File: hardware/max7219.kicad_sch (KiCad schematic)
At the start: 4 parts, among them U5 UDN2981A, U6 MAX7219, U7 ULN2803A, U8 74HC540

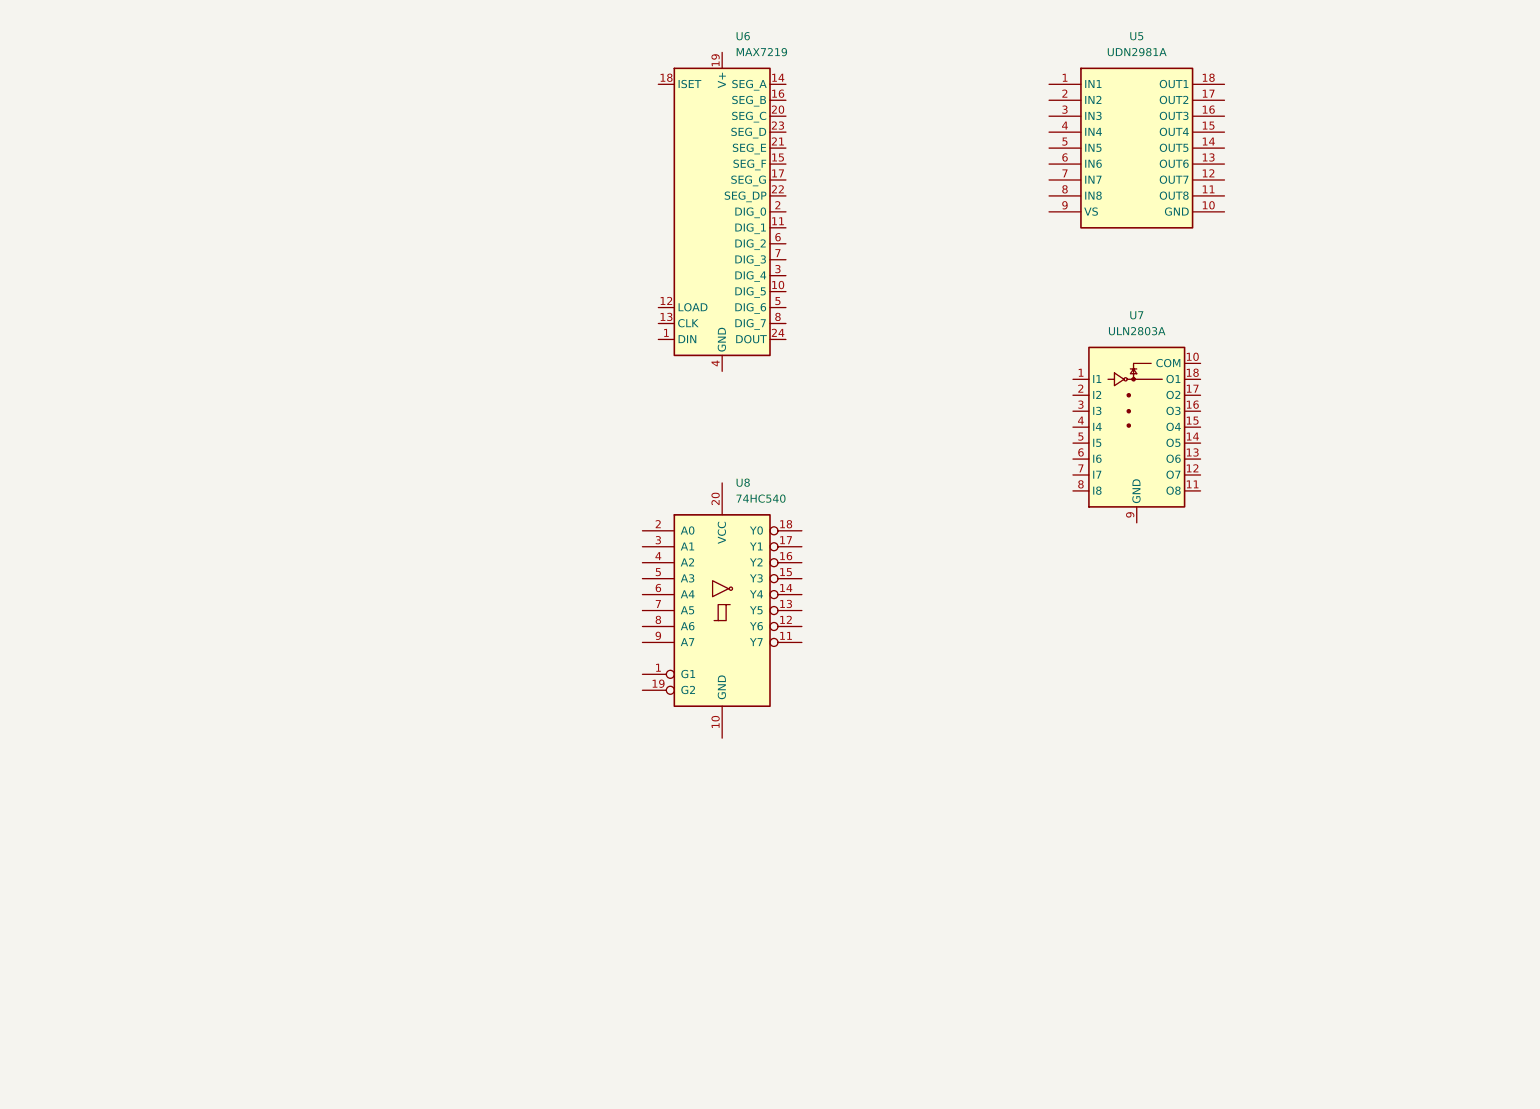
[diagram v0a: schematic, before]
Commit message: Hardware: Rename Temp to RTC-Sensor and Update Schematics
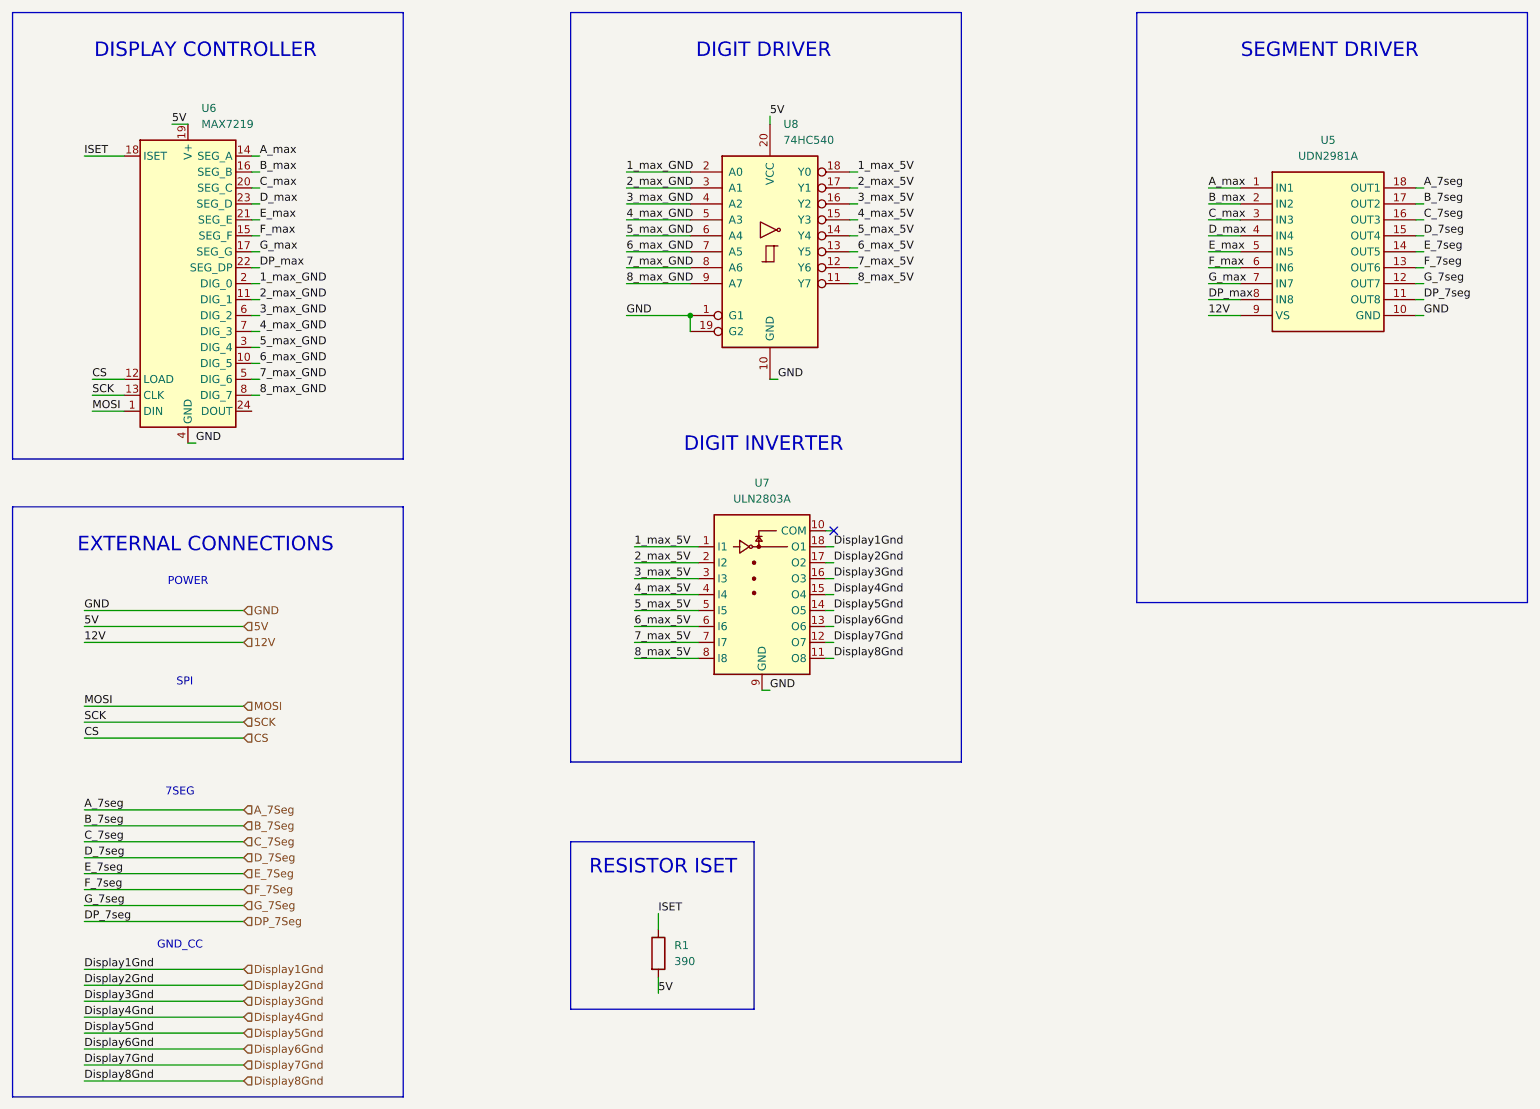
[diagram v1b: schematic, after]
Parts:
- added R1: 390, symbol Device:R
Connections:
- net GND: now reaches U8.1 (G1)
- net GND: now also U5.10 (GND), U6.4 (GND), U6.9 (GND), U7.9 (GND), U8.10 (GND), U8.19 (G2)
- net 8_max_5V: now reaches U8.11 (Y7)
- net 8_max_5V: now also U7.8 (I8)
- net 7_max_5V: now reaches U8.12 (Y6)
- net 7_max_5V: now also U7.7 (I7)
- net 6_max_5V: now reaches U8.13 (Y5)
- net 6_max_5V: now also U7.6 (I6)
- net 5_max_5V: now reaches U8.14 (Y4)
- net 5_max_5V: now also U7.5 (I5)
- net 4_max_5V: now reaches U8.15 (Y3)
- net 4_max_5V: now also U7.4 (I4)
- net 3_max_5V: now reaches U8.16 (Y2)
- net 3_max_5V: now also U7.3 (I3)
- net 2_max_5V: now reaches U8.17 (Y1)
- net 2_max_5V: now also U7.2 (I2)
- net 1_max_5V: now reaches U8.18 (Y0)
- net 1_max_5V: now also U7.1 (I1)
- net 1_max_GND: now reaches U8.2 (A0)
- net 1_max_GND: now also U6.2 (DIG_0)
- net 5V: now reaches U8.20 (VCC)
- net 5V: now also U6.19 (V+), R1.2
- net 2_max_GND: now reaches U8.3 (A1)
- net 2_max_GND: now also U6.11 (DIG_1)
- net 3_max_GND: now reaches U8.4 (A2)
- net 3_max_GND: now also U6.6 (DIG_2)
- net 4_max_GND: now reaches U8.5 (A3)
- net 4_max_GND: now also U6.7 (DIG_3)
- net 5_max_GND: now reaches U8.6 (A4)
- net 5_max_GND: now also U6.3 (DIG_4)
- net 6_max_GND: now reaches U8.7 (A5)
- net 6_max_GND: now also U6.10 (DIG_5)
- net 7_max_GND: now reaches U8.8 (A6)
- net 7_max_GND: now also U6.5 (DIG_6)
- net 8_max_GND: now reaches U8.9 (A7)
- net 8_max_GND: now also U6.8 (DIG_7)
- net A_max: now reaches U5.1 (IN1)
- net A_max: now also U6.14 (SEG_A)
- net DP_7Seg: now reaches U5.11 (OUT8)
- net G_7Seg: now reaches U5.12 (OUT7)
- net F_7Seg: now reaches U5.13 (OUT6)
- net E_7Seg: now reaches U5.14 (OUT5)
- net D_7Seg: now reaches U5.15 (OUT4)
- net C_7Seg: now reaches U5.16 (OUT3)
- net B_7Seg: now reaches U5.17 (OUT2)
- net A_7Seg: now reaches U5.18 (OUT1)
- net B_max: now reaches U5.2 (IN2)
- net B_max: now also U6.16 (SEG_B)
- net C_max: now reaches U5.3 (IN3)
- net C_max: now also U6.20 (SEG_C)
- net D_max: now reaches U5.4 (IN4)
- net D_max: now also U6.23 (SEG_D)
- net E_max: now reaches U5.5 (IN5)
- net E_max: now also U6.21 (SEG_E)
- net F_max: now reaches U5.6 (IN6)
- net F_max: now also U6.15 (SEG_F)
- net G_max: now reaches U5.7 (IN7)
- net G_max: now also U6.17 (SEG_G)
- net DP_max: now reaches U5.8 (IN8)
- net DP_max: now also U6.22 (SEG_DP)
- net 12V: now reaches U5.9 (VS)
- net MOSI: now reaches U6.1 (DIN)
- net CS: now reaches U6.12 (LOAD)
- net SCK: now reaches U6.13 (CLK)
- net ISET: now reaches U6.18 (ISET)
- net ISET: now also R1.1
- net Display8Gnd: now reaches U7.11 (O8)
- net Display7Gnd: now reaches U7.12 (O7)
- net Display6Gnd: now reaches U7.13 (O6)
- net Display5Gnd: now reaches U7.14 (O5)
- net Display4Gnd: now reaches U7.15 (O4)
- net Display3Gnd: now reaches U7.16 (O3)
- net Display2Gnd: now reaches U7.17 (O2)
- net Display1Gnd: now reaches U7.18 (O1)
- no-connect marks 0 -> 1
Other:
- note added: "7SEG"
- note added: "DIGIT DRIVER"
- note added: "DIGIT INVERTER"
- note added: "DISPLAY CONTROLLER"
- note added: "EXTERNAL CONNECTIONS"
- note added: "GND_CC"
- note added: "POWER"
- note added: "RESISTOR ISET"
- note added: "SEGMENT DRIVER"
- note added: "SPI"
- moved on the sheet: U5, U6, U7, U8

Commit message: Hardware: Updated Schematics and inicial ESP32 schematic
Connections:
- net CS renamed CS (LOAD)
- net MOSI renamed MOSI (DIN)
- net SCK renamed SCK (CLK)
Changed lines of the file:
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@@
 		)
 	)
-	(hierarchical_label "SCK"
+	(hierarchical_label "SCK (CLK)"
 		(shape input)
 		(at 59.69 132.08 0)
@@
 		)
 	)
-	(hierarchical_label "MOSI"
+	(hierarchical_label "MOSI (DIN)"
 		(shape input)
 		(at 59.69 129.54 0)
@@
 		)
 	)
-	(hierarchical_label "CS"
+	(hierarchical_label "CS (LOAD)"
 		(shape input)
 		(at 59.69 134.62 0)
